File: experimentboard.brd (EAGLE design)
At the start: 152.4 x 100 mm, 106 parts, among them IC1 TL072P, IC2 LM317, IC3 LM337, IC4 TL072P, U1 PCM1690, U2 DIR9001

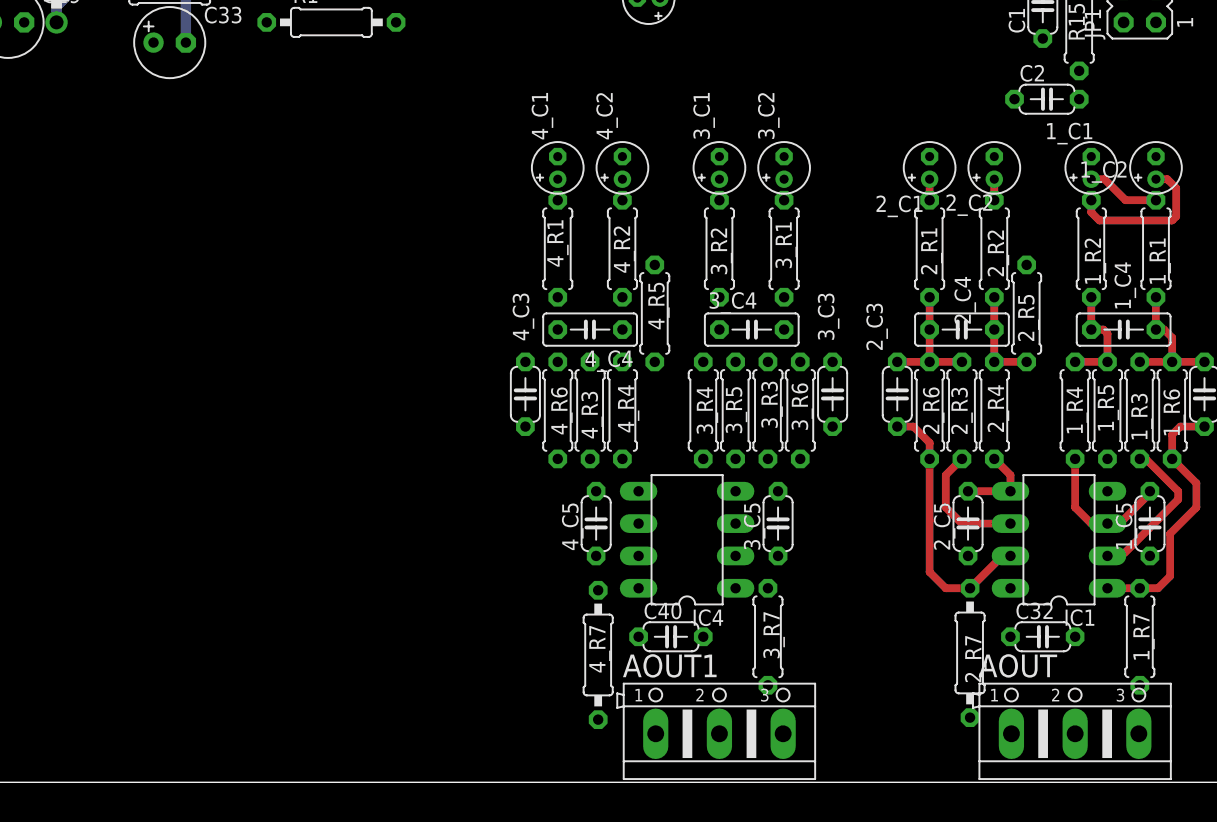
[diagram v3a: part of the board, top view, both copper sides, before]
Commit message: Added another analog output stage
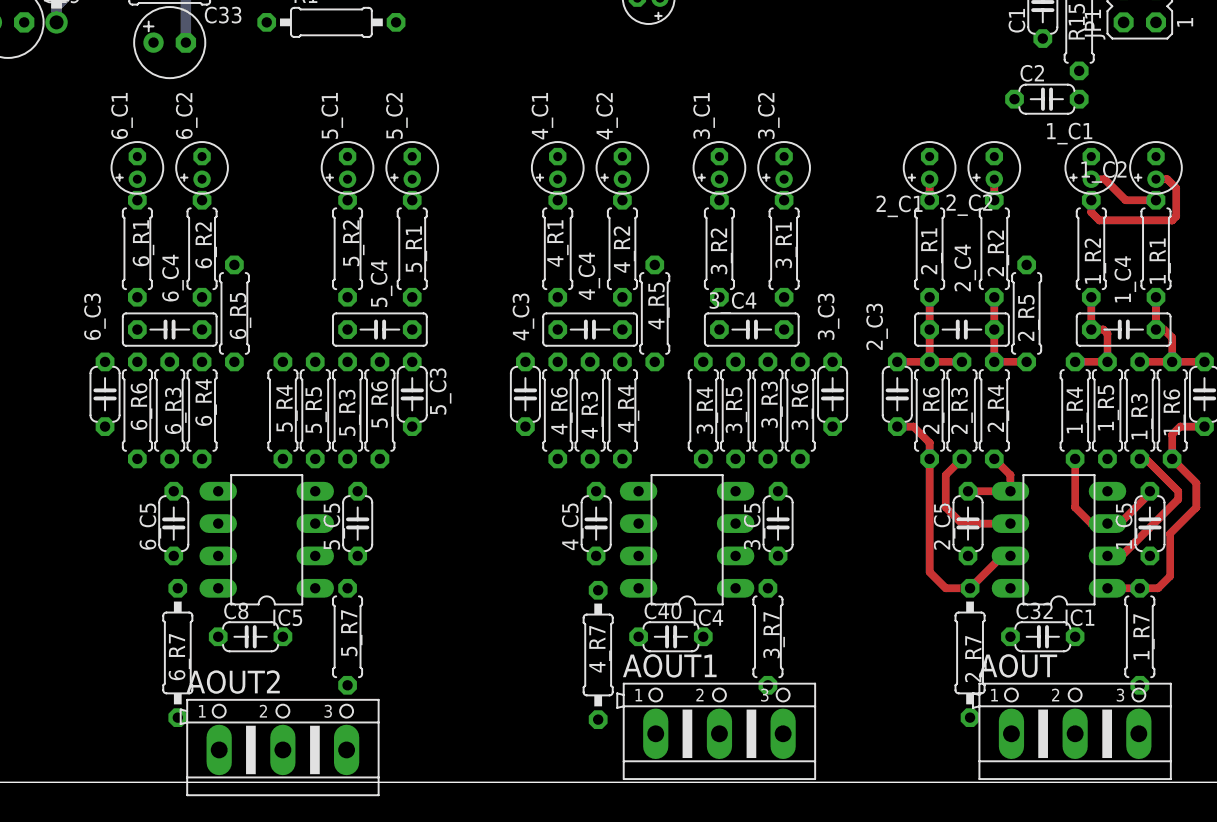
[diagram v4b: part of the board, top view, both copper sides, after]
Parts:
- added 5_C1, 5_C2, 6_C1, 6_C2: 10 µF, rcl:E1,8-4
- added 5_C3, 5_C5, 6_C3, 6_C5: 680pF, rcl:C050-024X044
- added 5_C4, 6_C4: 3.3nF, rcl:C050-025X075
- added 5_R1, 5_R2, 6_R1, 6_R2: 7.5k, rcl:0207/7
- added 5_R3, 5_R4, 6_R3, 6_R4: 360, rcl:0207/7
- added 5_R5, 5_R6, 6_R5, 6_R6: 5.6k, rcl:0207/7
- added 5_R7: 47, rcl:0207/7
- added 6_R7: 47, rcl:0207/10
- added AOUT2: (no value), con-ptr500:AK500/3
- added C8: 100nf, rcl:C050-024X044
- added IC5: TL072P, 0000halfgaar:DIL8
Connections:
- net N$28 renamed VOUT1+
- net N$29 renamed VOUT1-
- net N$35 renamed VOUT2-
- net N$36 renamed VOUT2+
- net N$46 renamed VOUT3+
- net N$47 renamed VOUT3-
- net N$59 renamed VOUT4-
- net N$60 renamed VOUT4+
- new net N$66: 5_C4.1, 5_R2.2, 5_R4.1, 5_R5.2
- new net N$67: 5_C3.1, 5_C4.2, 5_R1.2, 5_R3.1, 5_R6.1
- new net N$68: 5_C5.2, 5_R4.2, IC5.3
- new net N$69: 5_C3.2, 5_R6.2, 5_R7.1, IC5.1
- new net N$70: 5_R3.2, IC5.2
- new net N$71: 5_C2.+, 5_R2.1
- new net N$72: 5_C1.+, 5_R1.1
- new net N$75: 6_C4.1, 6_R2.2, 6_R4.1, 6_R5.2
- new net N$76: 6_C3.1, 6_C4.2, 6_R1.2, 6_R3.1, 6_R6.1
- new net N$77: 6_C5.2, 6_R4.2, IC5.5
- new net N$78: 6_C3.2, 6_R6.2, 6_R7.1, IC5.7
- new net N$79: 6_R3.2, IC5.6
- new net N$80: 6_C2.+, 6_R2.1
- new net N$81: 6_C1.+, 6_R1.1
- new net N$82: 5_R7.2, AOUT2.3
- new net N$83: 6_R7.2, AOUT2.1
- new net VOUT5+: 5_C1.-, U1.35
- new net VOUT5-: 5_C2.-, U1.36
- new net VOUT6+: 6_C1.-, U1.33
- new net VOUT6-: 6_C2.-, U1.34
- net AGND: now also 5_C5.1, 5_R5.1, 6_C5.1, 6_R5.1, AOUT2.2
- net V+: now also C8.1, IC5.8
- net V-: now also C8.2, IC5.4

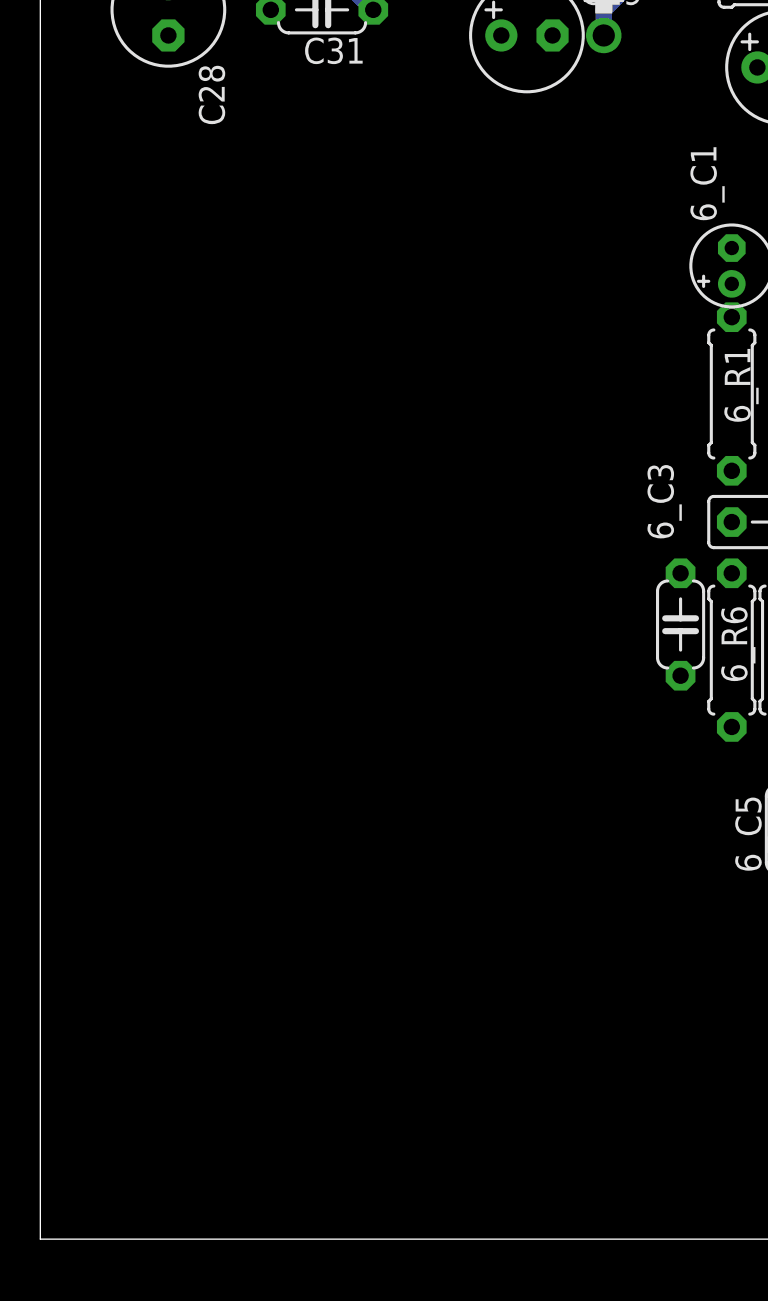
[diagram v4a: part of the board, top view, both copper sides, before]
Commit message: Added the last analog output stage
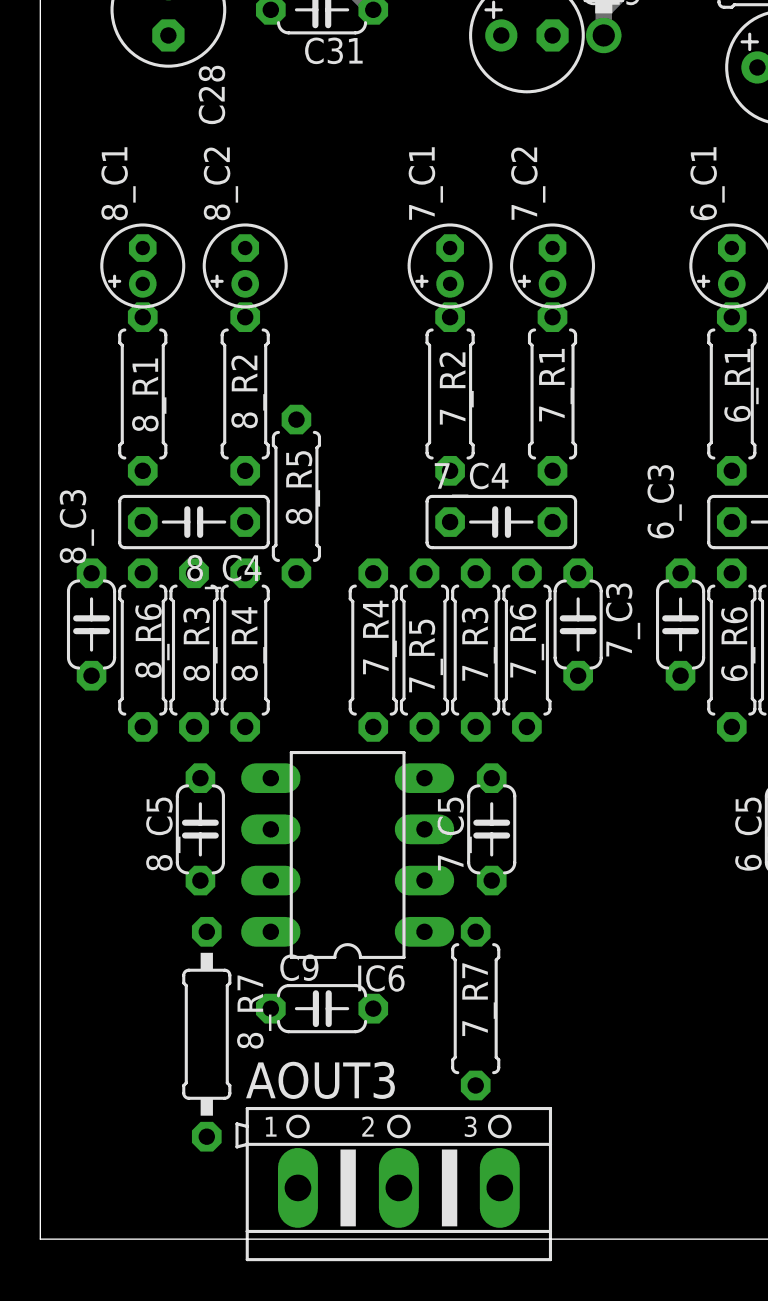
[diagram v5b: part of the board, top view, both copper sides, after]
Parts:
- added 7_C1, 7_C2, 8_C1, 8_C2: 10 µF, rcl:E1,8-4
- added 7_C3, 7_C5, 8_C3, 8_C5: 680pF, rcl:C050-024X044
- added 7_C4, 8_C4: 3.3nF, rcl:C050-025X075
- added 7_R1, 7_R2, 8_R1, 8_R2: 7.5k, rcl:0207/7
- added 7_R3, 7_R4, 8_R3, 8_R4: 360, rcl:0207/7
- added 7_R5, 7_R6, 8_R5, 8_R6: 5.6k, rcl:0207/7
- added 7_R7: 47, rcl:0207/7
- added 8_R7: 47, rcl:0207/10
- added AOUT3: (no value), con-ptr500:AK500/3
- added C9: 100nf, rcl:C050-024X044
- added IC6: TL072P, 0000halfgaar:DIL8
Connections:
- new net N$29: 7_C4.1, 7_R2.2, 7_R4.1, 7_R5.2
- new net N$35: 7_C3.1, 7_C4.2, 7_R1.2, 7_R3.1, 7_R6.1
- new net N$36: 7_C5.2, 7_R4.2, IC6.3
- new net N$46: 7_C3.2, 7_R6.2, 7_R7.1, IC6.1
- new net N$47: 7_R3.2, IC6.2
- new net N$59: 7_C2.+, 7_R2.1
- new net N$60: 7_C1.+, 7_R1.1
- new net N$73: 8_C4.1, 8_R2.2, 8_R4.1, 8_R5.2
- new net N$74: 8_C3.1, 8_C4.2, 8_R1.2, 8_R3.1, 8_R6.1
- new net N$84: 8_C5.2, 8_R4.2, IC6.5
- new net N$85: 8_C3.2, 8_R6.2, 8_R7.1, IC6.7
- new net N$86: 8_R3.2, IC6.6
- new net N$87: 8_C2.+, 8_R2.1
- new net N$88: 8_C1.+, 8_R1.1
- new net N$89: 7_R7.2, AOUT3.3
- new net N$90: 8_R7.2, AOUT3.1
- new net VOUT7+: 7_C1.-, U1.31
- new net VOUT7-: 7_C2.-, U1.32
- new net VOUT8+: 8_C1.-, U1.29
- new net VOUT8-: 8_C2.-, U1.30
- net AGND: now also 7_C5.1, 7_R5.1, 8_C5.1, 8_R5.1, AOUT3.2
- net V+: now also C9.1, IC6.8
- net V-: now also C9.2, IC6.4

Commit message: Working on EEPROM and TOSLINK
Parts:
- added C10, C11: 100nf, rcl:C050-024X044
- added L1: 47uH, rcl:0207/10
- added R2, R8, R9: 5.6k, rcl:0207/7
- added U$1: PLR135/T9, 0000halfgaar:PLR135/T9
- added U3: CAT24C256, 0000halfgaar:TSSOP8
- moved C7 9.25 mm to (113.0, 78.3)
- moved C2 8.82 mm to (98.1, 58.1), turned to 270 degrees
- moved C15 4.58 mm to (97.6, 67.5)
- moved R30 4.58 mm to (106.5, 76.5)
- moved R32 4.58 mm to (101.1, 76.5)
- moved C1 4.58 mm to (101.6, 58.4)
- moved JP1 4.58 mm to (109.2, 58.4)
- moved R15 4.58 mm to (104.5, 57.1)
- moved JP2 4.58 mm to (96.5, 74.9)
- moved U2 4.58 mm to (104.1, 67.3)
- moved R31 4.58 mm to (103.8, 76.5)
- moved C5 2.54 mm to (93.2, 67.6)
- moved C6 2.54 mm to (90.6, 65.6)
- moved R39 2.54 mm to (74.9, 73.7)
- moved C3 2.54 mm to (74.5, 59.1)
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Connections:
- new net CAPE_I2C_SCL: R8.1, U$2.19, U3.6
- new net CAPE_I2C_SDA: R2.1, U$2.20, U3.5
- net DGND: now also C10.1, C11.1, U$1.2, U3.4
- net N$20: now also U$1.1
- net N$54: now also R9.1, U3.3; no longer U2.4
- net VDD: now also C10.2, C11.2, L1.1, L1.2, R2.2, R8.2, R9.2, U$1.3, U3.8
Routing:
- net DIR_AUDIO: track 0.00 -> 50.9 mm
- net ACLKR: track 0.00 -> 38.1 mm
- net DOUT: track 0.00 -> 25.0 mm
- net RST: track 0.00 -> 24.3 mm
- net MCLK: track 0.00 -> 21.8 mm
- net AHCLKX: track 0.00 -> 19.2 mm
- net CAPE_I2C_SDA: track 0.00 -> 16.3 mm, vias 0 -> 1
- net FSR: track 0.00 -> 14.9 mm
- net CAPE_I2C_SCL: track 0.00 -> 12.6 mm, vias 0 -> 1
- net N$63: track 0.00 -> 7.21 mm
- net N$53: track 0.00 -> 5.44 mm
- net N$62: track 0.00 -> 5.27 mm
- net N$61: track 0.00 -> 4.65 mm
- net N$5: track 0.00 -> 4.51 mm
- net N$52: track 0.00 -> 3.57 mm
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
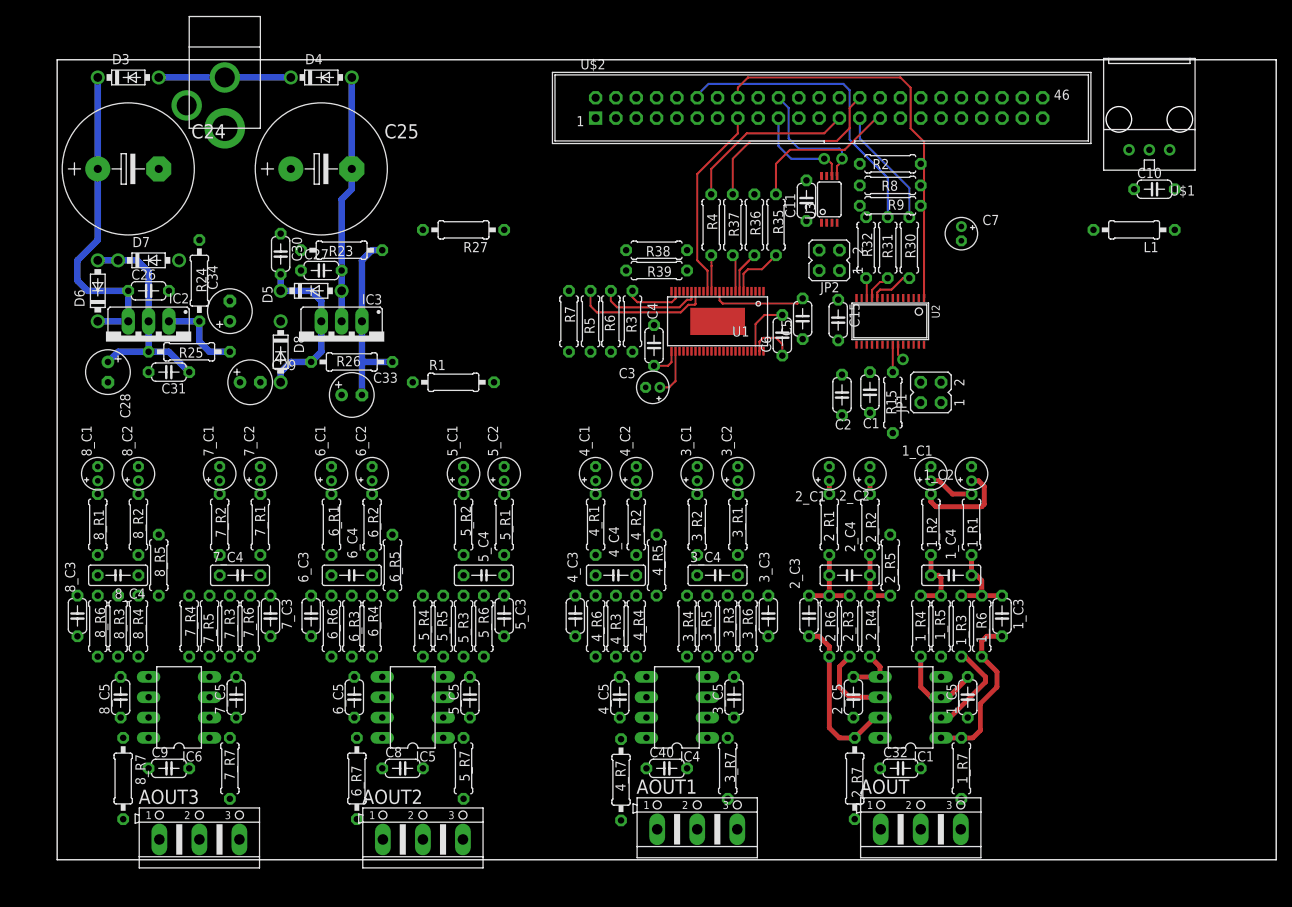
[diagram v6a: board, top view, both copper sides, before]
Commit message: Mostly the analog section, routing and squeezing
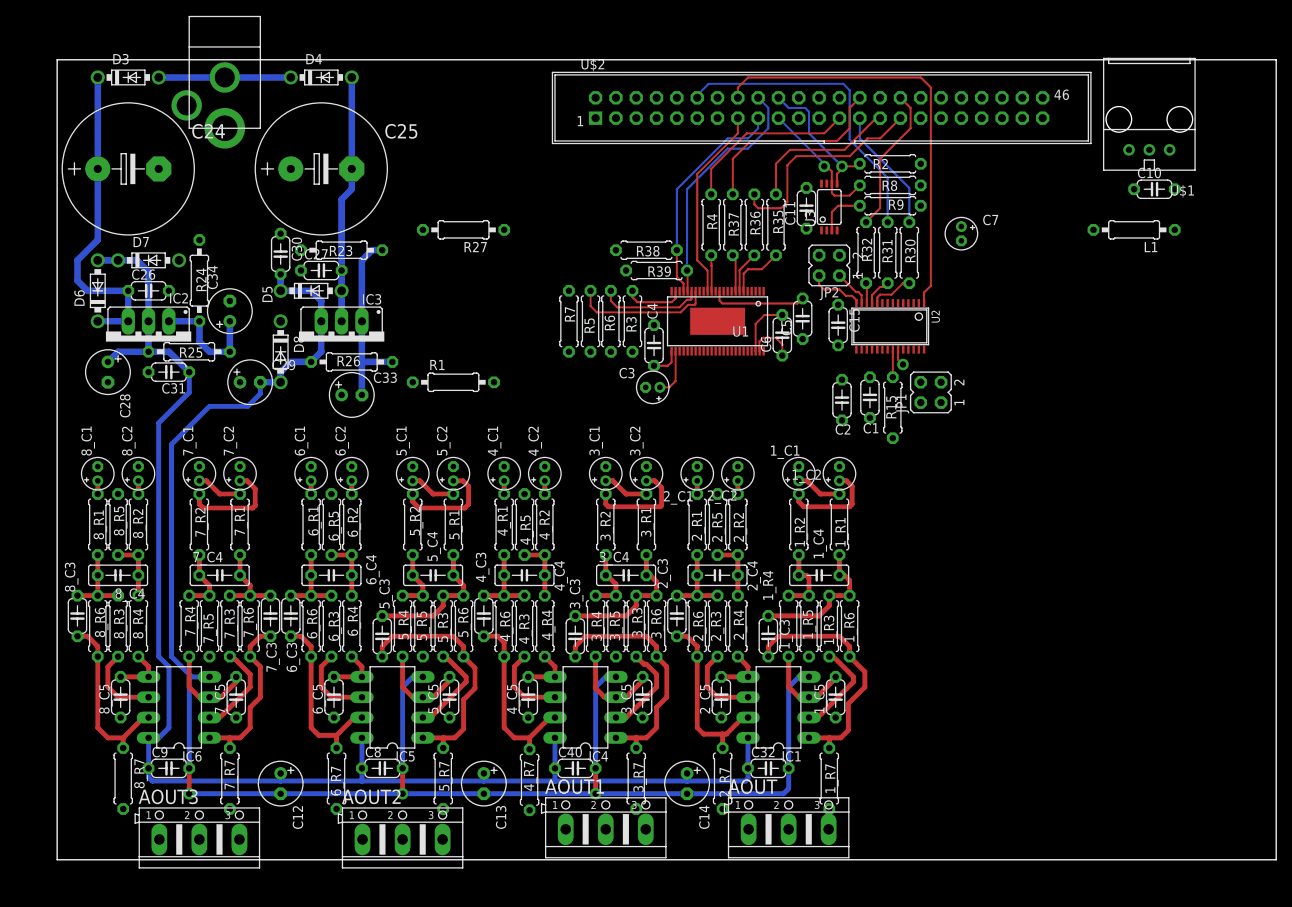
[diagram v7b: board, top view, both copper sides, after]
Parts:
- added C12, C13, C14: 100uF/25V, rcl:E2,5-6
- 2_R7, 4_R7, 6_R7, 8_R7: device rcl:0207/10 -> rcl:0207/7
- moved 1_C3 29.3 mm to (88.9, 27.9)
- moved 3_C3 24.3 mm to (64.8, 27.9)
- moved 2_R5 22.2 mm to (82.5, 41.9)
- moved 4_R5 17.3 mm to (58.4, 41.9)
- moved 1_R7 16.6 mm to (96.5, 10.2)
- moved 1_C1 16.5 mm to (92.7, 48.3)
- moved 1_C4 16.5 mm to (95.2, 35.6)
- moved 1_C5 16.5 mm to (97.3, 20.3)
- moved 1_R2 16.5 mm to (92.7, 41.9)
- moved 1_R3 16.5 mm to (96.5, 29.2)
- moved 1_R4 16.5 mm to (91.4, 29.2)
- moved 2_C3 16.5 mm to (77.5, 30.5)
- moved 2_C4 16.5 mm to (82.5, 35.6)
- moved 2_R3 16.5 mm to (82.5, 29.2)
- moved AOUT 16.5 mm to (91.4, 3.81)
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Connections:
- net V+: now also C12.+, C13.+, C14.+
- net V-: now also C12.-, C13.-, C14.-
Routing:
- net V-: track 21.4 -> 210.0 mm, vias 0 -> 3
- net V+: track 28.7 -> 177.2 mm
- net N$69: track 0.00 -> 30.8 mm
- net N$21: track 0.00 -> 30.6 mm
- net SDA: track 0.00 -> 30.4 mm
- net SCL: track 0.00 -> 27.7 mm
- net ACLKX: track 0.00 -> 27.1 mm
- net N$55: track 0.00 -> 22.9 mm
- net N$78: track 0.00 -> 22.5 mm
- net N$85: track 0.00 -> 22.4 mm
- net N$46: track 0.00 -> 21.2 mm
- net DIN: track 0.00 -> 18.4 mm
- net N$10: track 0.00 -> 17.8 mm
- net N$67: track 0.00 -> 17.6 mm
- net N$59: track 0.00 -> 13.0 mm
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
